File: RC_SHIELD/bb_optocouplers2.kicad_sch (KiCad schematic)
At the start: 48 parts, among them U1 SFH6345, U2 SFH6345

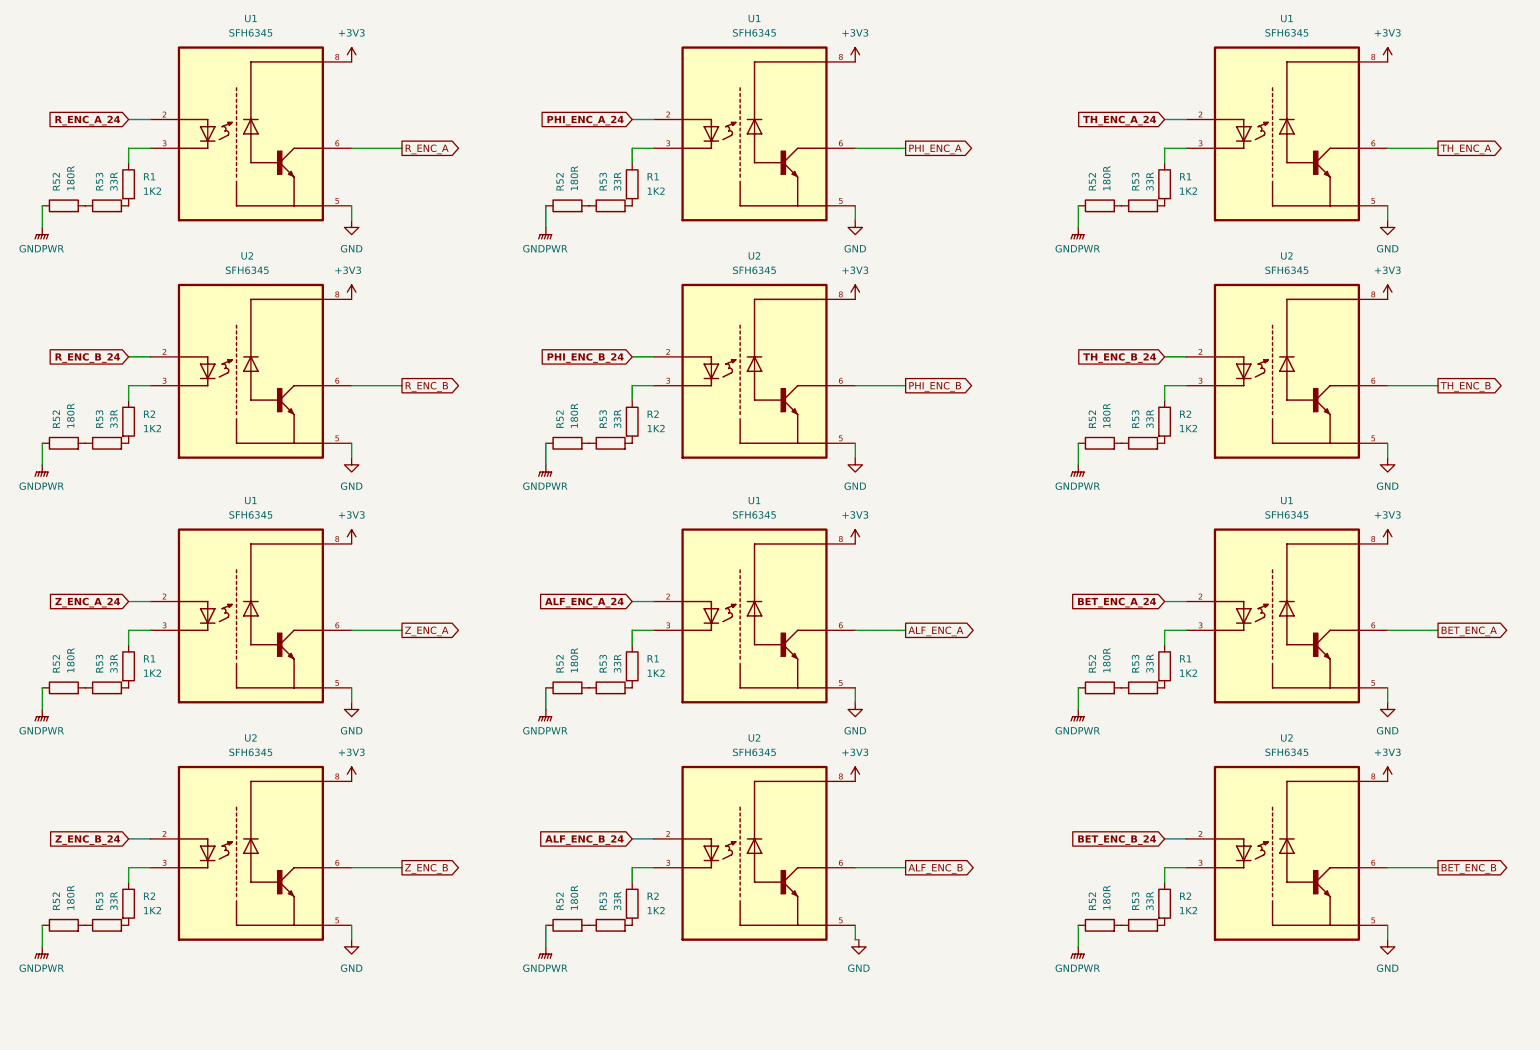
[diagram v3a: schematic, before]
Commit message: [SCH] reorganized optocouplers and tidied up page 2
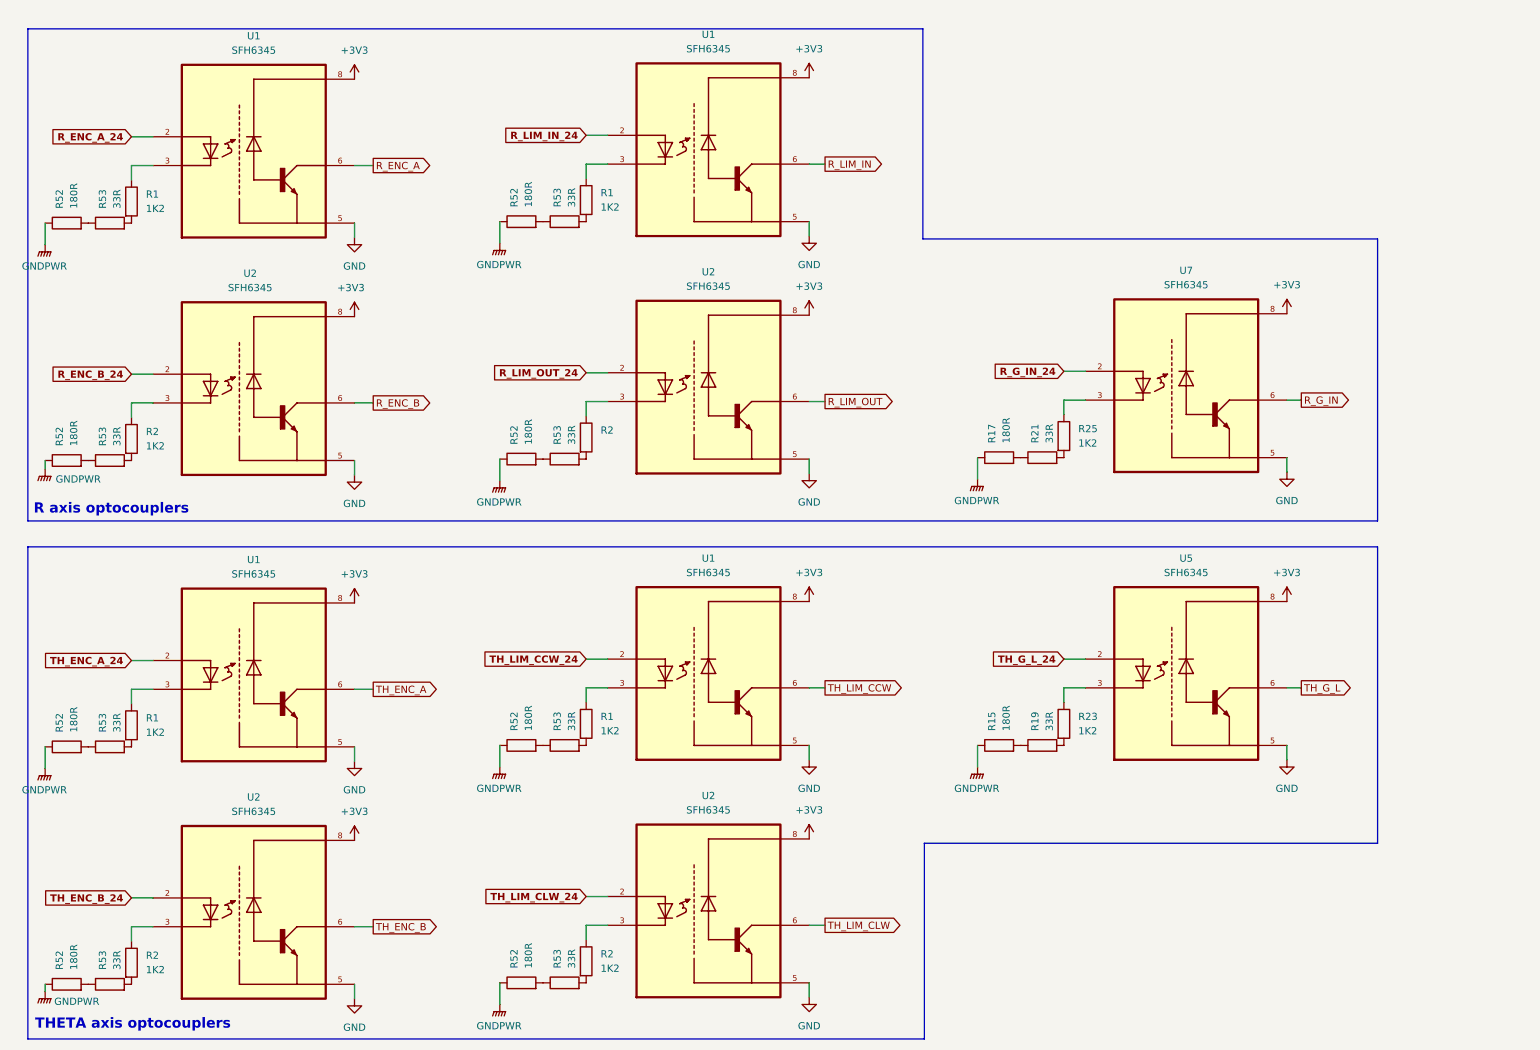
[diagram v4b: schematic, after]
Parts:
- removed R1 (x4), R2 (x4): 1K2, Resistor_SMD:R_0805_2012Metric_Pad1.20x1.40mm_HandSolder, symbol Device:R
- removed R52 (x8): 180R, Resistor_SMD:R_0805_2012Metric_Pad1.20x1.40mm_HandSolder, symbol Device:R
- removed R53 (x8): 33R, Resistor_SMD:R_0805_2012Metric_Pad1.20x1.40mm_HandSolder, symbol Device:R
- removed U1 (x4), U2 (x4): SFH6345, SFH6345:DIP762W50P254L977H451Q8, symbol SFH6345:SFH6345
- added R1 (x2), R2 (x2), R23, R25: 1K2, Resistor_SMD:R_0805_2012Metric_Pad1.20x1.40mm_HandSolder, symbol Device:R
- added R15, R17, R52 (x4): 180R, Resistor_SMD:R_0805_2012Metric_Pad1.20x1.40mm_HandSolder, symbol Device:R
- added R19, R21, R53 (x4): 33R, Resistor_SMD:R_0805_2012Metric_Pad1.20x1.40mm_HandSolder, symbol Device:R
- added U1 (x2), U2 (x2), U5, U7: SFH6345, SFH6345:DIP762W50P254L977H451Q8, symbol SFH6345:SFH6345
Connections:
- net +3V3: now also U1.8, U1.8, U2.8, U2.8, U5.8, U7.8
- net GND: now also U1.5, U1.5, U2.5, U2.5, U5.5, U7.5
- net GNDPWR: now also R15.1, R17.1, R52.1, R52.1, R52.1, R52.1
- new net: R15.2, R19.1
- new net: R19.2, R23.2
- new net: R2.1, U2.3 (x2)
- new net: R2.2, R53.2 (x2)
- new net: R52.2, R53.1 (x4)
- new net: R17.2, R21.1
- new net: R23.1, U5.3
- new net: R1.1, U1.3 (x2)
- new net: R1.2, R53.2 (x2)
- new net: R25.1, U7.3
- new net: R21.2, R25.2
- new net R_G_IN: U7.6
- new net R_G_IN_24: U7.2
- new net R_LIM_IN: U1.6
- new net R_LIM_IN_24: U1.2
- new net R_LIM_OUT: U2.6
- new net R_LIM_OUT_24: U2.2
- new net TH_G_L: U5.6
- new net TH_G_L_24: U5.2
- new net TH_LIM_CCW: U1.6
- new net TH_LIM_CCW_24: U1.2
- new net TH_LIM_CLW: U2.6
- new net TH_LIM_CLW_24: U2.2
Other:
- note added: "R axis optocouplers"
- note added: "THETA axis optocouplers"
- title: Karcsi (INDACT Robot Arm) - Encoder optocouplers -> Karcsi (INDACT Robot Arm) - R & THETA axes optocouplers
- moved on the sheet: R1, R2, R52, R53, U1, U2

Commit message: Revert "[SCH] reorganized optocouplers and tidied up page 2"
This reverts commit 005640e4067293c5014d1b79d289b32d97da3ff9.
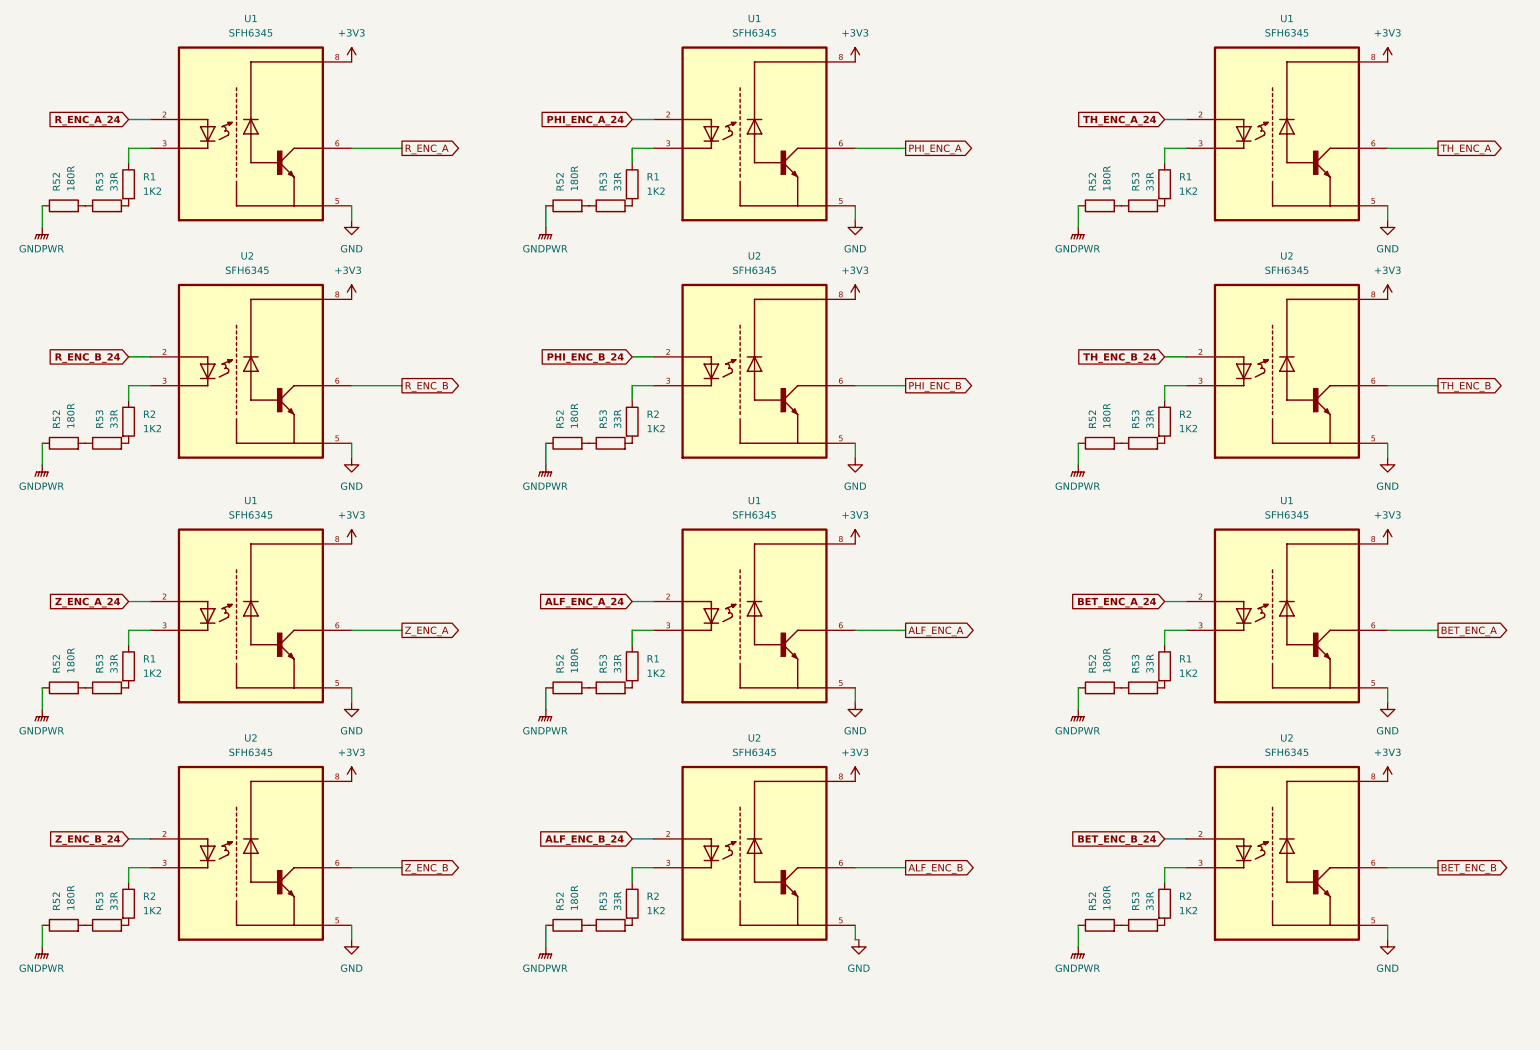
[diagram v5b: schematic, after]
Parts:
- removed R1 (x2), R2 (x2), R23, R25: 1K2, Resistor_SMD:R_0805_2012Metric_Pad1.20x1.40mm_HandSolder, symbol Device:R
- removed R15, R17, R52 (x4): 180R, Resistor_SMD:R_0805_2012Metric_Pad1.20x1.40mm_HandSolder, symbol Device:R
- removed R19, R21, R53 (x4): 33R, Resistor_SMD:R_0805_2012Metric_Pad1.20x1.40mm_HandSolder, symbol Device:R
- removed U1 (x2), U2 (x2), U5, U7: SFH6345, SFH6345:DIP762W50P254L977H451Q8, symbol SFH6345:SFH6345
- added R1 (x4), R2 (x4): 1K2, Resistor_SMD:R_0805_2012Metric_Pad1.20x1.40mm_HandSolder, symbol Device:R
- added R52 (x8): 180R, Resistor_SMD:R_0805_2012Metric_Pad1.20x1.40mm_HandSolder, symbol Device:R
- added R53 (x8): 33R, Resistor_SMD:R_0805_2012Metric_Pad1.20x1.40mm_HandSolder, symbol Device:R
- added U1 (x4), U2 (x4): SFH6345, SFH6345:DIP762W50P254L977H451Q8, symbol SFH6345:SFH6345
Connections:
- net +3V3: now also U1.8, U1.8, U1.8, U1.8, U2.8, U2.8, U2.8, U2.8
- net GND: now also U1.5, U1.5, U1.5, U1.5, U2.5, U2.5, U2.5, U2.5
- net GNDPWR: now also R52.1, R52.1, R52.1, R52.1, R52.1, R52.1, R52.1, R52.1
- new net: R2.1, U2.3 (x4)
- new net: R52.2, R53.1 (x8)
- new net: R2.2, R53.2 (x4)
- new net: R1.2, R53.2 (x4)
- new net: R1.1, U1.3 (x4)
- new net ALF_ENC_A: U1.6
- new net ALF_ENC_A_24: U1.2
- new net ALF_ENC_B: U2.6
- new net ALF_ENC_B_24: U2.2
- new net BET_ENC_A: U1.6
- new net BET_ENC_A_24: U1.2
- new net BET_ENC_B: U2.6
- new net BET_ENC_B_24: U2.2
- new net PHI_ENC_A: U1.6
- new net PHI_ENC_A_24: U1.2
- new net PHI_ENC_B: U2.6
- new net PHI_ENC_B_24: U2.2
- new net Z_ENC_A: U1.6
- new net Z_ENC_A_24: U1.2
- new net Z_ENC_B: U2.6
- new net Z_ENC_B_24: U2.2
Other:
- note removed: "R axis optocouplers"
- note removed: "THETA axis optocouplers"
- title: Karcsi (INDACT Robot Arm) - R & THETA axes optocouplers -> Karcsi (INDACT Robot Arm) - Encoder optocouplers
- moved on the sheet: R1, R2, R52, R53, U1, U2
